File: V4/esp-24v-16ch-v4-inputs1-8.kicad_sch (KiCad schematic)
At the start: 10 parts, among them U10 OR-3H7-4

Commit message: Revising schematics
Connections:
- net +3.3V renamed +3V3
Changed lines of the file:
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@@
 			)
 		)
-		(property "Value" "+3.3V"
+		(property "Value" "+3V3"
 			(at 194.691 76.8858 0)
 			(effects

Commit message: Revising the schematics
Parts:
- R31: value 2k2/62,5mW -> 2k2
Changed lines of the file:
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@@
 			)
 		)
-		(property "Value" "2k2/62,5mW"
+		(property "Value" "2k2"
 			(at 196.85 82.55 0)
 			(effects

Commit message: Rerouting
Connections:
- net INFILTER: now reaches C28.1, D10.1 (K), R30.1
- net INPRE: now reaches D8.1 (A1), FB1.2, R29.1, R30.2
- net INLED: now reaches D9.2 (A), R29.2
- net INOPTO: now reaches D10.2 (A), U10.1
- net MUX_IN renamed MUXIN
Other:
- moved on the sheet: D10, D9, R31, U10A

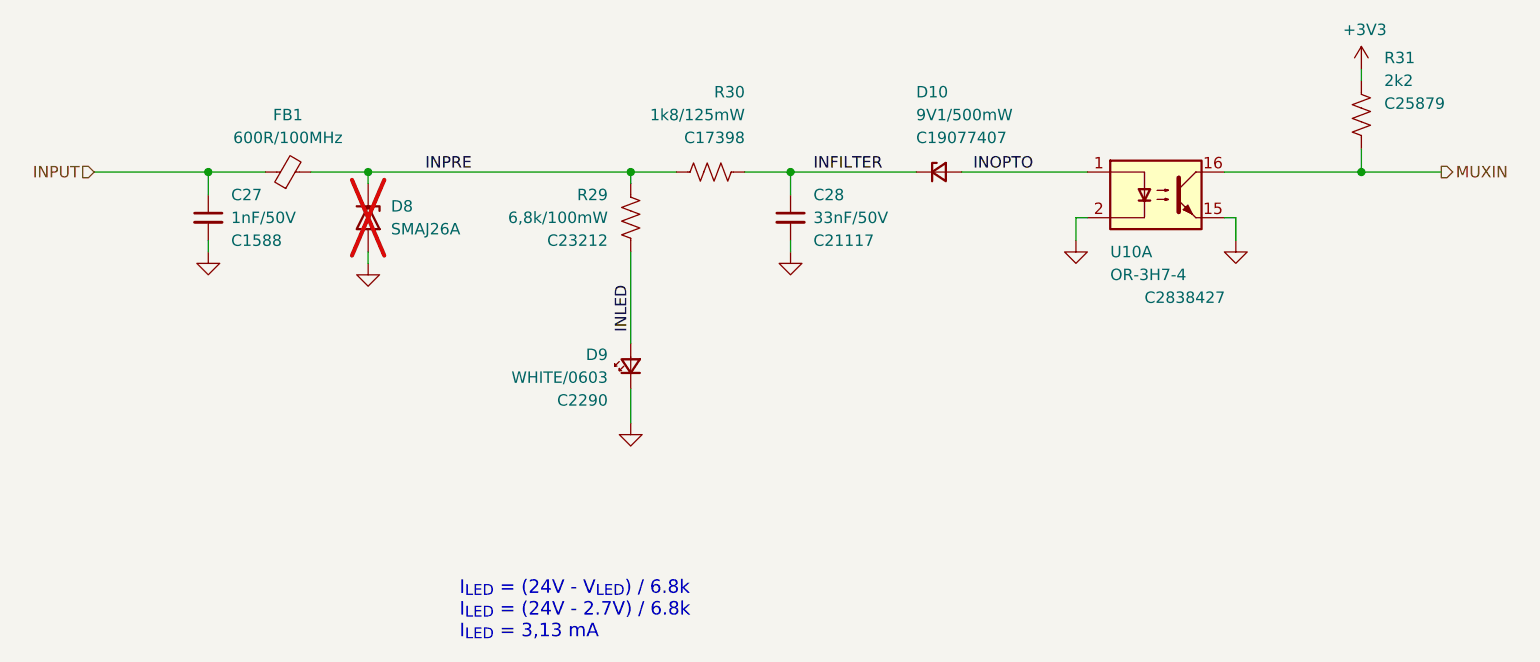
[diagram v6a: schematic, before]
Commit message: Rerouting
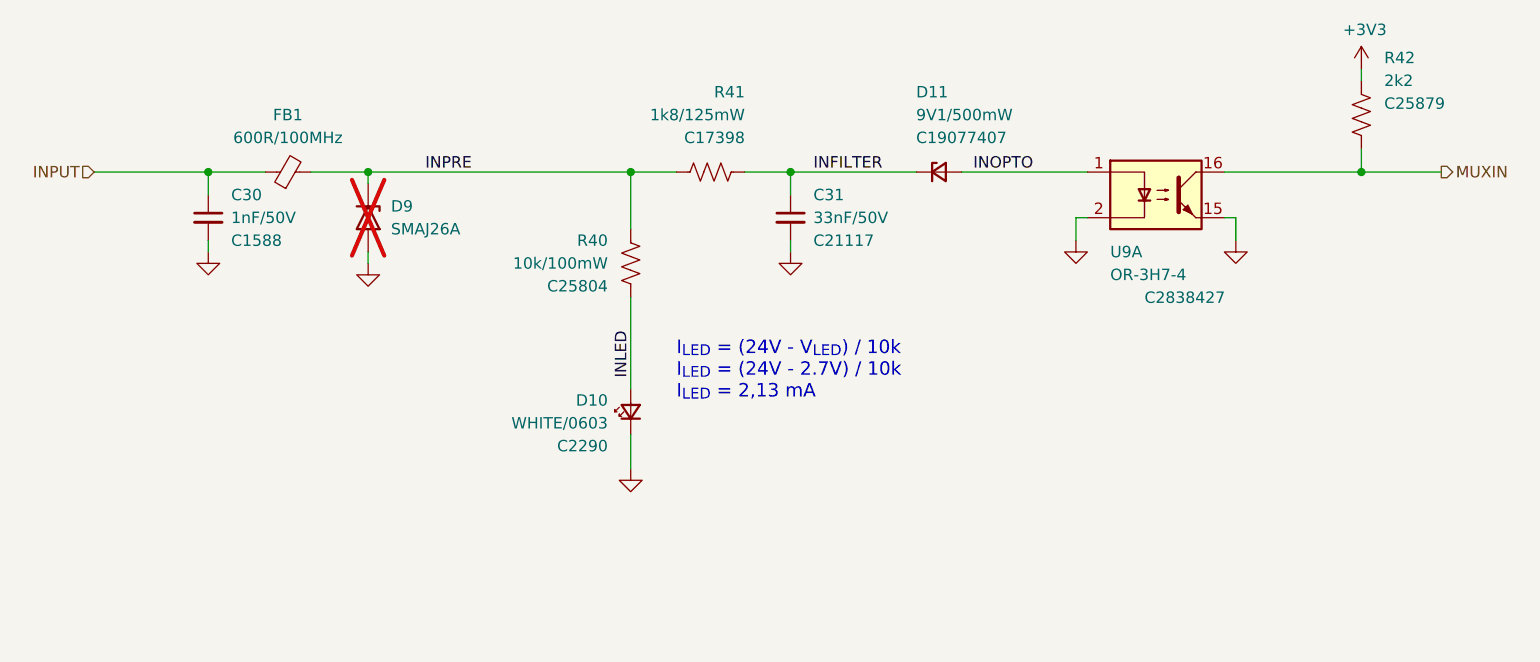
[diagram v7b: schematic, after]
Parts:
- removed C27: 1nF/50V, Tales:C_0603_1608Metric, symbol Device:C_Small
- removed C28: 33nF/50V, Tales:C_0603_1608Metric, symbol Device:C_Small
- removed D10: 9V1/500mW, Tales:D_SOD-123, symbol Device:D_Zener_Small
- removed D8: SMAJ26A, Diode_SMD:D_SMA, symbol Diode:SMAJ26A
- removed D9: WHITE/0603, Tales:LED_0603_1608Metric, symbol Device:LED_Small
- removed R29: 6,8k/100mW, Tales:R_0603_1608Metric, symbol Device:R_US
- removed R30: 1k8/125mW, Tales:R_0805_2012Metric, symbol Device:R_US
- removed R31: 2k2, Tales:R_0402_1005Metric, symbol Device:R_US
- removed U10: OR-3H7-4, Tales:SOP-16_4.4x10.4mm_P1.27mm, symbol Tales:OR-3H7-4
- added C30: 1nF/50V, Tales:C_0603_1608Metric, symbol Device:C_Small
- added C31: 33nF/50V, Tales:C_0603_1608Metric, symbol Device:C_Small
- added D10: WHITE/0603, Tales:LED_0603_1608Metric, symbol Device:LED_Small
- added D11: 9V1/500mW, Tales:D_SOD-123, symbol Device:D_Zener_Small
- added D9: SMAJ26A, Diode_SMD:D_SMA, symbol Diode:SMAJ26A
- added R40: 10k/100mW, Tales:R_0603_1608Metric, symbol Device:R_US
- added R41: 1k8/125mW, Tales:R_0805_2012Metric, symbol Device:R_US
- added R42: 2k2, Tales:R_0402_1005Metric, symbol Device:R_US
- added U9: OR-3H7-4, Tales:SOP-16_4.4x10.4mm_P1.27mm, symbol Tales:OR-3H7-4
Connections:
- net +3V3: now also R42.1
- net GND: now also C30.2, C31.2, D10.1 (K), D9.2 (A2), U9.15, U9.2
- net INFILTER: now also C31.1, D11.1 (K), R41.1
- net INLED: now also D10.2 (A), R40.2
- net INOPTO: now also D11.2 (A), U9.1
- net INPRE: now also D9.1 (A1), R40.1, R41.2
- net INPUT: now also C30.1
- net MUXIN: now also R42.2, U9.16
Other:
- note added: "I_{LED} = (24V - V_{LED}) / 10k I_{LED} = (24V - 2.7V) / 10k I_{LED} = 2,13 mA"
- note removed: "I_{LED} = (24V - V_{LED}) / 6.8k I_{LED} = (24V - 2.7V) / 6.8k I_{LED} = 3,13 mA"
